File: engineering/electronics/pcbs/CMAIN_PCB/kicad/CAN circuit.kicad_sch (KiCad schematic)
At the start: 17 parts, among them U1 TJA1049T/3J, U2 MCP2515-I/SO, X1 16MHz

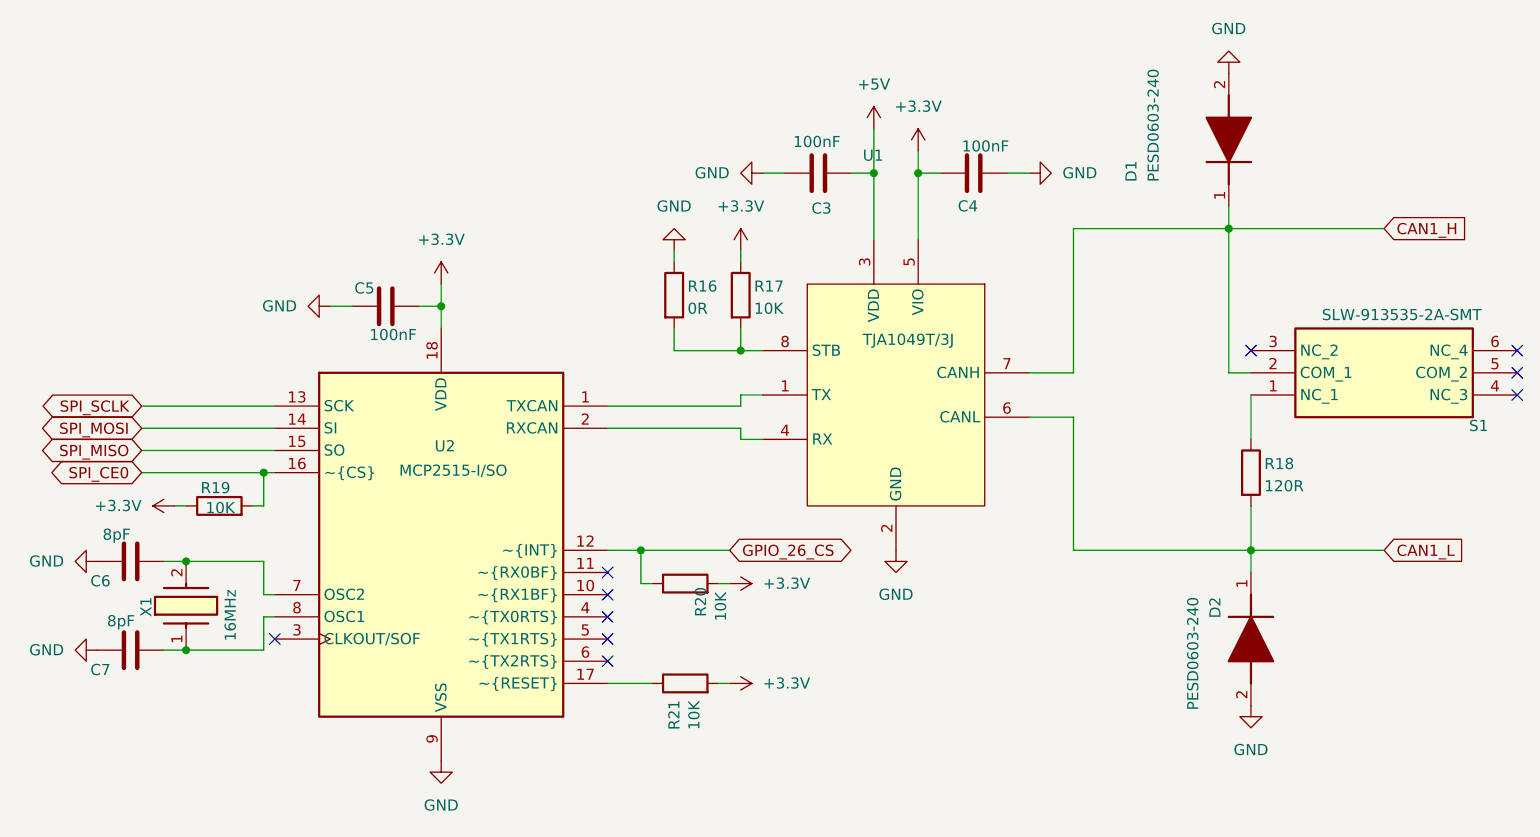
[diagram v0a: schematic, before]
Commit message: Import linked CMAIN PCB layout
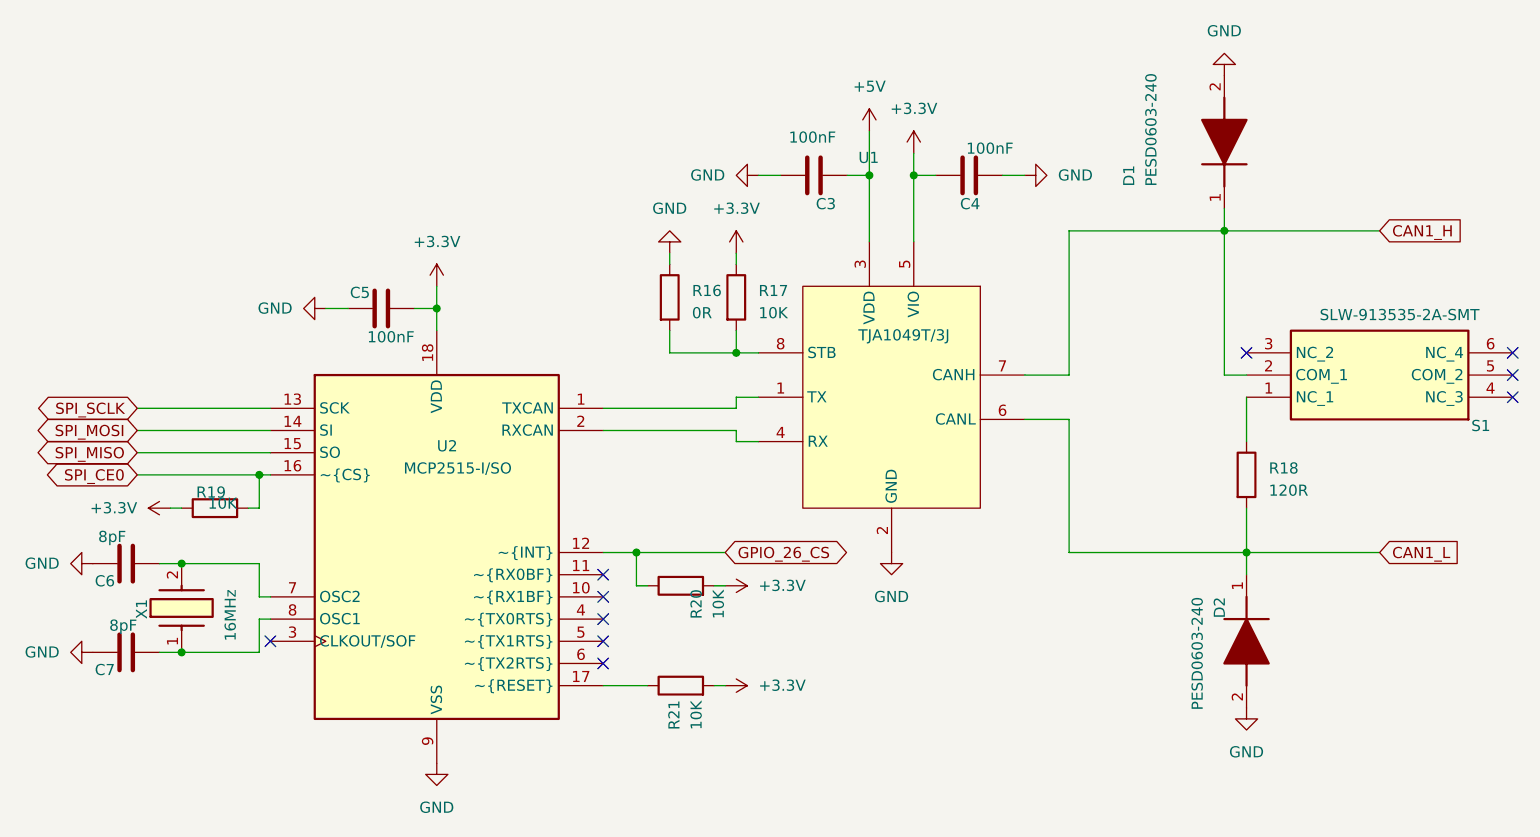
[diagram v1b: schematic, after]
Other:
- moved on the sheet: C3, C4, C5, C6, C7, D1, D2, R16, R17, R18, R19, R20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

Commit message: electronics: clean up CMAIN local libraries
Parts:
- C3, C4, C5: footprint Capacitor_SMD:C_0805_2012Metric_Pad1.18x1.45mm_HandSolder -> CMAIN_PCB:C_0805_2012Metric_Pad1.18x1.45mm_HandSolder
- C6, C7: footprint Capacitor_SMD:C_0603_1608Metric_Pad1.08x0.95mm_HandSolder -> CMAIN_PCB:C_0603_1608Metric_Pad1.08x0.95mm_HandSolder
- D1, D2: footprint Samacsys:DIONC1608X55N -> CMAIN_PCB:DIONC1608X55N
- R16, R17, R18, R19, R20, R21: footprint Resistor_SMD:R_0805_2012Metric_Pad1.20x1.40mm_HandSolder -> CMAIN_PCB:R_0805_2012Metric_Pad1.20x1.40mm_HandSolder
- X1: footprint Samacsys:NX3225GB-16M-STD-CRA-2 -> CMAIN_PCB:NX3225GB-16M-STD-CRA-2
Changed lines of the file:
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@@
 			)
 		)
-		(property "Footprint" "Resistor_SMD:R_0805_2012Metric_Pad1.20x1.40mm_HandSolder"
+		(property "Footprint" "CMAIN_PCB:R_0805_2012Metric_Pad1.20x1.40mm_HandSolder"
 			(at 91.44 106.68 90)
 			(hide yes)
@@
 			)
 		)
-		(property "Footprint" "Capacitor_SMD:C_0603_1608Metric_Pad1.08x0.95mm_HandSolder"
+		(property "Footprint" "CMAIN_PCB:C_0603_1608Metric_Pad1.08x0.95mm_HandSolder"
 			(at 85.09 120.65 0)
 			(hide yes)
@@
 			)
 		)
-		(property "Footprint" "Samacsys:NX3225GB-16M-STD-CRA-2"
+		(property "Footprint" "CMAIN_PCB:NX3225GB-16M-STD-CRA-2"
 			(at 184.15 113.03 0)
 			(hide yes)
@@
 			)
 		)
-		(property "Footprint" "Capacitor_SMD:C_0805_2012Metric_Pad1.18x1.45mm_HandSolder"
+		(property "Footprint" "CMAIN_PCB:C_0805_2012Metric_Pad1.18x1.45mm_HandSolder"
 			(at 163.83 66.04 0)
 			(hide yes)
@@
 			)
 		)
-		(property "Footprint" "Capacitor_SMD:C_0805_2012Metric_Pad1.18x1.45mm_HandSolder"
+		(property "Footprint" "CMAIN_PCB:C_0805_2012Metric_Pad1.18x1.45mm_HandSolder"
 			(at 181.61 66.04 0)
 			(hide yes)
@@
 			)
 		)
-		(property "Footprint" "Resistor_SMD:R_0805_2012Metric_Pad1.20x1.40mm_HandSolder"
+		(property "Footprint" "CMAIN_PCB:R_0805_2012Metric_Pad1.20x1.40mm_HandSolder"
 			(at 144.78 115.57 90)
 			(hide yes)
@@
 			)
 		)
-		(property "Footprint" "Samacsys:DIONC1608X55N"
+		(property "Footprint" "CMAIN_PCB:DIONC1608X55N"
 			(at 113.03 124.46 0)
 			(hide yes)
@@
 			)
 		)
-		(property "Footprint" "Resistor_SMD:R_0805_2012Metric_Pad1.20x1.40mm_HandSolder"
+		(property "Footprint" "CMAIN_PCB:R_0805_2012Metric_Pad1.20x1.40mm_HandSolder"
 			(at 149.86 81.28 90)
 			(hide yes)
@@
 			)
 		)
-		(property "Footprint" "Samacsys:DIONC1608X55N"
+		(property "Footprint" "CMAIN_PCB:DIONC1608X55N"
 			(at 304.8 59.69 0)
 			(hide yes)
@@
 			)
 		)
-		(property "Footprint" "Resistor_SMD:R_0805_2012Metric_Pad1.20x1.40mm_HandSolder"
+		(property "Footprint" "CMAIN_PCB:R_0805_2012Metric_Pad1.20x1.40mm_HandSolder"
 			(at 208.28 101.6 90)
 			(hide yes)
@@
 			)
 		)
-		(property "Footprint" "Resistor_SMD:R_0805_2012Metric_Pad1.20x1.40mm_HandSolder"
+		(property "Footprint" "CMAIN_PCB:R_0805_2012Metric_Pad1.20x1.40mm_HandSolder"
 			(at 142.24 81.28 90)
 			(hide yes)
@@
 			)
 		)
-		(property "Footprint" "Resistor_SMD:R_0805_2012Metric_Pad1.20x1.40mm_HandSolder"
+		(property "Footprint" "CMAIN_PCB:R_0805_2012Metric_Pad1.20x1.40mm_HandSolder"
 			(at 144.78 127 90)
 			(hide yes)
@@
 			)
 		)
-		(property "Footprint" "Capacitor_SMD:C_0603_1608Metric_Pad1.08x0.95mm_HandSolder"
+		(property "Footprint" "CMAIN_PCB:C_0603_1608Metric_Pad1.08x0.95mm_HandSolder"
 			(at 85.09 110.49 0)
 			(hide yes)
@@
 			)
 		)
-		(property "Footprint" "Capacitor_SMD:C_0805_2012Metric_Pad1.18x1.45mm_HandSolder"
+		(property "Footprint" "CMAIN_PCB:C_0805_2012Metric_Pad1.18x1.45mm_HandSolder"
 			(at 114.3 81.28 0)
 			(hide yes)

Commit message: electronics: update CMAIN PCB from June layout
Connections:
- net +5V renamed 5V_1
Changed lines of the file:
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@@
 			)
 		)
-		(property "Value" "+5V"
+		(property "Value" "5V_1"
 			(at 166.37 57.15 0)
 			(show_name no)

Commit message: electronics: shorten CMAIN footprint filenames for Windows
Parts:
- C3, C4, C5: footprint CMAIN_PCB:C_0805_2012Metric_Pad1.18x1.45mm_HandSolder -> CMAIN_PCB:fp_71505040a9
- C6, C7: footprint CMAIN_PCB:C_0603_1608Metric_Pad1.08x0.95mm_HandSolder -> CMAIN_PCB:fp_6a12138141
- R16, R17, R18, R19, R20, R21: footprint CMAIN_PCB:R_0805_2012Metric_Pad1.20x1.40mm_HandSolder -> CMAIN_PCB:fp_9fb50b8536
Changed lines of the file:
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@@
 			)
 		)
-		(property "Footprint" "CMAIN_PCB:R_0805_2012Metric_Pad1.20x1.40mm_HandSolder"
+		(property "Footprint" "CMAIN_PCB:fp_9fb50b8536"
 			(at 91.44 106.68 90)
 			(hide yes)
@@
 			)
 		)
-		(property "Footprint" "CMAIN_PCB:C_0603_1608Metric_Pad1.08x0.95mm_HandSolder"
+		(property "Footprint" "CMAIN_PCB:fp_6a12138141"
 			(at 85.09 120.65 0)
 			(hide yes)
@@
 			)
 		)
-		(property "Footprint" "CMAIN_PCB:C_0805_2012Metric_Pad1.18x1.45mm_HandSolder"
+		(property "Footprint" "CMAIN_PCB:fp_71505040a9"
 			(at 163.83 66.04 0)
 			(hide yes)
@@
 			)
 		)
-		(property "Footprint" "CMAIN_PCB:C_0805_2012Metric_Pad1.18x1.45mm_HandSolder"
+		(property "Footprint" "CMAIN_PCB:fp_71505040a9"
 			(at 181.61 66.04 0)
 			(hide yes)
@@
 			)
 		)
-		(property "Footprint" "CMAIN_PCB:R_0805_2012Metric_Pad1.20x1.40mm_HandSolder"
+		(property "Footprint" "CMAIN_PCB:fp_9fb50b8536"
 			(at 144.78 115.57 90)
 			(hide yes)
@@
 			)
 		)
-		(property "Footprint" "CMAIN_PCB:R_0805_2012Metric_Pad1.20x1.40mm_HandSolder"
+		(property "Footprint" "CMAIN_PCB:fp_9fb50b8536"
 			(at 149.86 81.28 90)
 			(hide yes)
@@
 			)
 		)
-		(property "Footprint" "CMAIN_PCB:R_0805_2012Metric_Pad1.20x1.40mm_HandSolder"
+		(property "Footprint" "CMAIN_PCB:fp_9fb50b8536"
 			(at 208.28 101.6 90)
 			(hide yes)
@@
 			)
 		)
-		(property "Footprint" "CMAIN_PCB:R_0805_2012Metric_Pad1.20x1.40mm_HandSolder"
+		(property "Footprint" "CMAIN_PCB:fp_9fb50b8536"
 			(at 142.24 81.28 90)
 			(hide yes)
@@
 			)
 		)
-		(property "Footprint" "CMAIN_PCB:R_0805_2012Metric_Pad1.20x1.40mm_HandSolder"
+		(property "Footprint" "CMAIN_PCB:fp_9fb50b8536"
 			(at 144.78 127 90)
 			(hide yes)
@@
 			)
 		)
-		(property "Footprint" "CMAIN_PCB:C_0603_1608Metric_Pad1.08x0.95mm_HandSolder"
+		(property "Footprint" "CMAIN_PCB:fp_6a12138141"
 			(at 85.09 110.49 0)
 			(hide yes)
@@
 			)
 		)
-		(property "Footprint" "CMAIN_PCB:C_0805_2012Metric_Pad1.18x1.45mm_HandSolder"
+		(property "Footprint" "CMAIN_PCB:fp_71505040a9"
 			(at 114.3 81.28 0)
 			(hide yes)

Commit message: electronics: integrate CMAIN STEP updates and consolidate footprints
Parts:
- S1: footprint Samacsys:SLW9135352ASMT -> CMAIN_PCB:SLW9135352ASMT
- U1: footprint Samacsys:SOIC127P600X175-8N -> CMAIN_PCB:SOIC127P600X175-8N
- U2: footprint Samacsys:SOIC127P1030X265-18N -> CMAIN_PCB:SOIC127P1030X265-18N
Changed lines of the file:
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@@
 			)
 		)
-		(property "Footprint" "Samacsys:SOIC127P1030X265-18N"
+		(property "Footprint" "CMAIN_PCB:SOIC127P1030X265-18N"
 			(at 130.81 176.53 0)
 			(hide yes)
@@
 			)
 		)
-		(property "Footprint" "Samacsys:SLW9135352ASMT"
+		(property "Footprint" "CMAIN_PCB:SLW9135352ASMT"
 			(at 213.36 -2.54 0)
 			(hide yes)
@@
 			)
 		)
-		(property "Footprint" "Samacsys:SOIC127P600X175-8N"
+		(property "Footprint" "CMAIN_PCB:SOIC127P600X175-8N"
 			(at 182.88 173.99 0)
 			(hide yes)

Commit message: Clean up CMAIN part value fields
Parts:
- C3, C4, C5: value 100nF -> 100nF 50V; footprint CMAIN_PCB:fp_71505040a9 -> Capacitor_SMD:C_0805_2012Metric_Pad1.18x1.45mm_HandSolder
- C6, C7: value 8pF -> 8pF 50V; footprint CMAIN_PCB:fp_6a12138141 -> Capacitor_SMD:C_0603_1608Metric_Pad1.08x0.95mm_HandSolder
- R16: value 0R -> 0R 150V; footprint CMAIN_PCB:fp_9fb50b8536 -> Resistor_SMD:R_0805_2012Metric_Pad1.20x1.40mm_HandSolder
- R17, R19, R20, R21: value 10K -> 10K 150V; footprint CMAIN_PCB:fp_9fb50b8536 -> Resistor_SMD:R_0805_2012Metric_Pad1.20x1.40mm_HandSolder
- R18: value 120R -> 120R 150V; footprint CMAIN_PCB:fp_9fb50b8536 -> Resistor_SMD:R_0805_2012Metric_Pad1.20x1.40mm_HandSolder
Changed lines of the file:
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@@
 			)
 		)
-		(property "Value" "10K"
+		(property "Value" "10K 150V"
 			(at 93.98 104.14 90)
 			(show_name no)
@@
 			)
 		)
-		(property "Footprint" "CMAIN_PCB:fp_9fb50b8536"
+		(property "Footprint" "Resistor_SMD:R_0805_2012Metric_Pad1.20x1.40mm_HandSolder"
 			(at 91.44 106.68 90)
 			(hide yes)
@@
 			)
 		)
-		(property "Value" "8pF"
+		(property "Value" "8pF 50V"
 			(at 82.55 118.11 90)
 			(show_name no)
@@
 			)
 		)
-		(property "Footprint" "CMAIN_PCB:fp_6a12138141"
+		(property "Footprint" "Capacitor_SMD:C_0603_1608Metric_Pad1.08x0.95mm_HandSolder"
 			(at 85.09 120.65 0)
 			(hide yes)
@@
 			)
 		)
-		(property "Value" "100nF"
+		(property "Value" "100nF 50V"
 			(at 162.56 62.23 90)
 			(show_name no)
@@
 			)
 		)
-		(property "Footprint" "CMAIN_PCB:fp_71505040a9"
+		(property "Footprint" "Capacitor_SMD:C_0805_2012Metric_Pad1.18x1.45mm_HandSolder"
 			(at 163.83 66.04 0)
 			(hide yes)
@@
 			)
 		)
-		(property "Value" "100nF"
+		(property "Value" "100nF 50V"
 			(at 182.88 63.5 90)
 			(show_name no)
@@
 			)
 		)
-		(property "Footprint" "CMAIN_PCB:fp_71505040a9"
+		(property "Footprint" "Capacitor_SMD:C_0805_2012Metric_Pad1.18x1.45mm_HandSolder"
 			(at 181.61 66.04 0)
 			(hide yes)
@@
 			)
 		)
-		(property "Value" "10K"
+		(property "Value" "10K 150V"
 			(at 149.86 118.11 0)
 			(show_name no)
@@
 			)
 		)
-		(property "Footprint" "CMAIN_PCB:fp_9fb50b8536"
+		(property "Footprint" "Resistor_SMD:R_0805_2012Metric_Pad1.20x1.40mm_HandSolder"
 			(at 144.78 115.57 90)
 			(hide yes)
@@
 			)
 		)
-		(property "Value" "10K"
+		(property "Value" "10K 150V"
 			(at 153.67 83.82 0)
 			(show_name no)
@@
 			)
 		)
-		(property "Footprint" "CMAIN_PCB:fp_9fb50b8536"
+		(property "Footprint" "Resistor_SMD:R_0805_2012Metric_Pad1.20x1.40mm_HandSolder"
 			(at 149.86 81.28 90)
 			(hide yes)
@@
 			)
 		)
-		(property "Value" "120R"
+		(property "Value" "120R 150V"
 			(at 212.09 104.14 0)
 			(show_name no)
@@
 			)
 		)
-		(property "Footprint" "CMAIN_PCB:fp_9fb50b8536"
+		(property "Footprint" "Resistor_SMD:R_0805_2012Metric_Pad1.20x1.40mm_HandSolder"
 			(at 208.28 101.6 90)
 			(hide yes)
@@
 			)
 		)
-		(property "Value" "0R"
+		(property "Value" "0R 150V"
 			(at 146.05 83.82 0)
 			(show_name no)
@@
 			)
 		)
-		(property "Footprint" "CMAIN_PCB:fp_9fb50b8536"
+		(property "Footprint" "Resistor_SMD:R_0805_2012Metric_Pad1.20x1.40mm_HandSolder"
 			(at 142.24 81.28 90)
 			(hide yes)
@@
 			)
 		)
-		(property "Value" "10K"
+		(property "Value" "10K 150V"
 			(at 147.32 130.81 0)
 			(show_name no)
@@
 			)
 		)
-		(property "Footprint" "CMAIN_PCB:fp_9fb50b8536"
+		(property "Footprint" "Resistor_SMD:R_0805_2012Metric_Pad1.20x1.40mm_HandSolder"
 			(at 144.78 127 90)
 			(hide yes)
@@
 			)
 		)
-		(property "Value" "8pF"
+		(property "Value" "8pF 50V"
 			(at 81.28 107.95 90)
 			(show_name no)
@@
 			)
 		)
-		(property "Footprint" "CMAIN_PCB:fp_6a12138141"
+		(property "Footprint" "Capacitor_SMD:C_0603_1608Metric_Pad1.08x0.95mm_HandSolder"
 			(at 85.09 110.49 0)
 			(hide yes)
@@
 			)
 		)
-		(property "Value" "100nF"
+		(property "Value" "100nF 50V"
 			(at 114.3 85.09 90)
 			(show_name no)
@@
 			)
 		)
-		(property "Footprint" "CMAIN_PCB:fp_71505040a9"
+		(property "Footprint" "Capacitor_SMD:C_0805_2012Metric_Pad1.18x1.45mm_HandSolder"
 			(at 114.3 81.28 0)
 			(hide yes)
